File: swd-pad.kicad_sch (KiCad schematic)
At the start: 4 parts, among them J6 OroConn6p

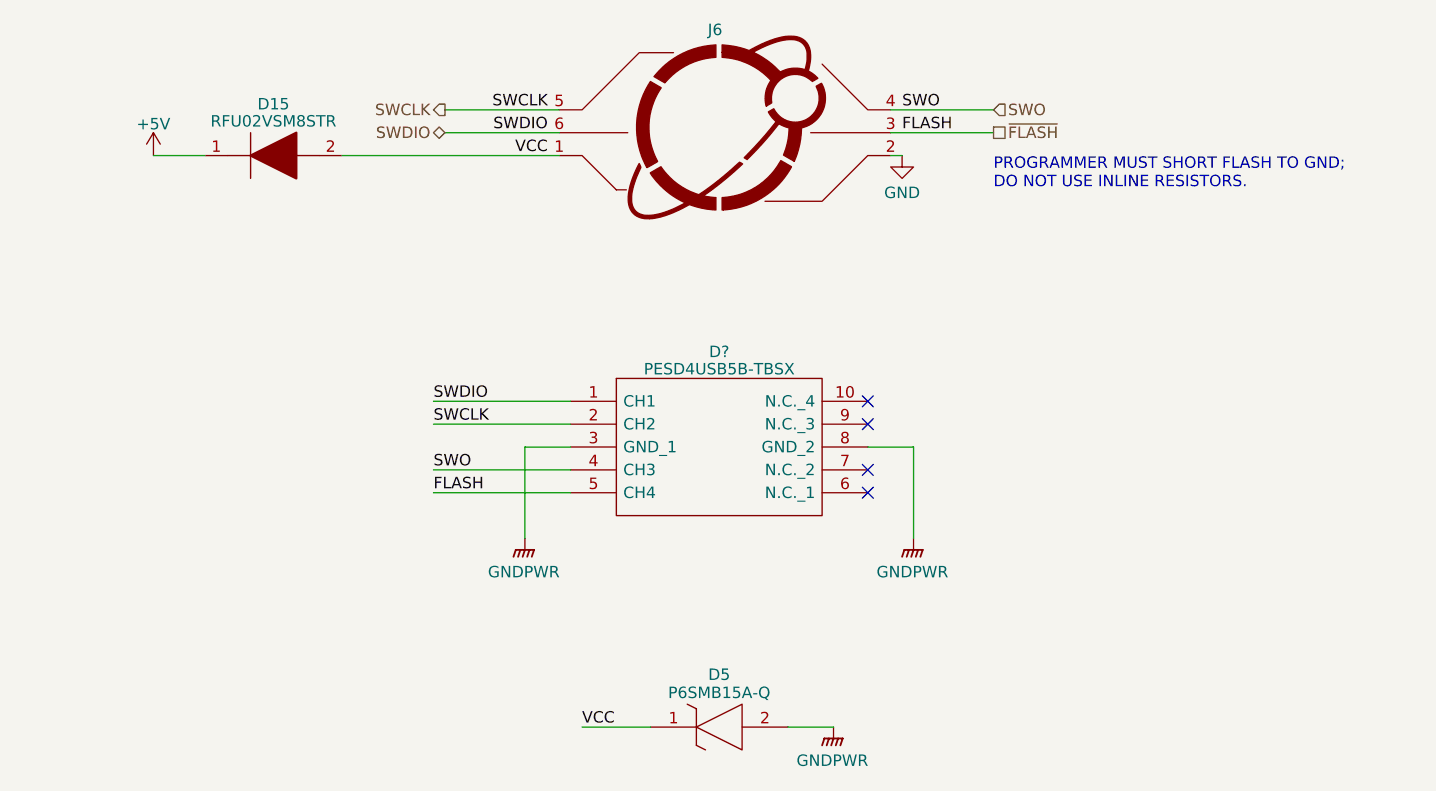
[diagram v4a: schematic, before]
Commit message: initial component layout
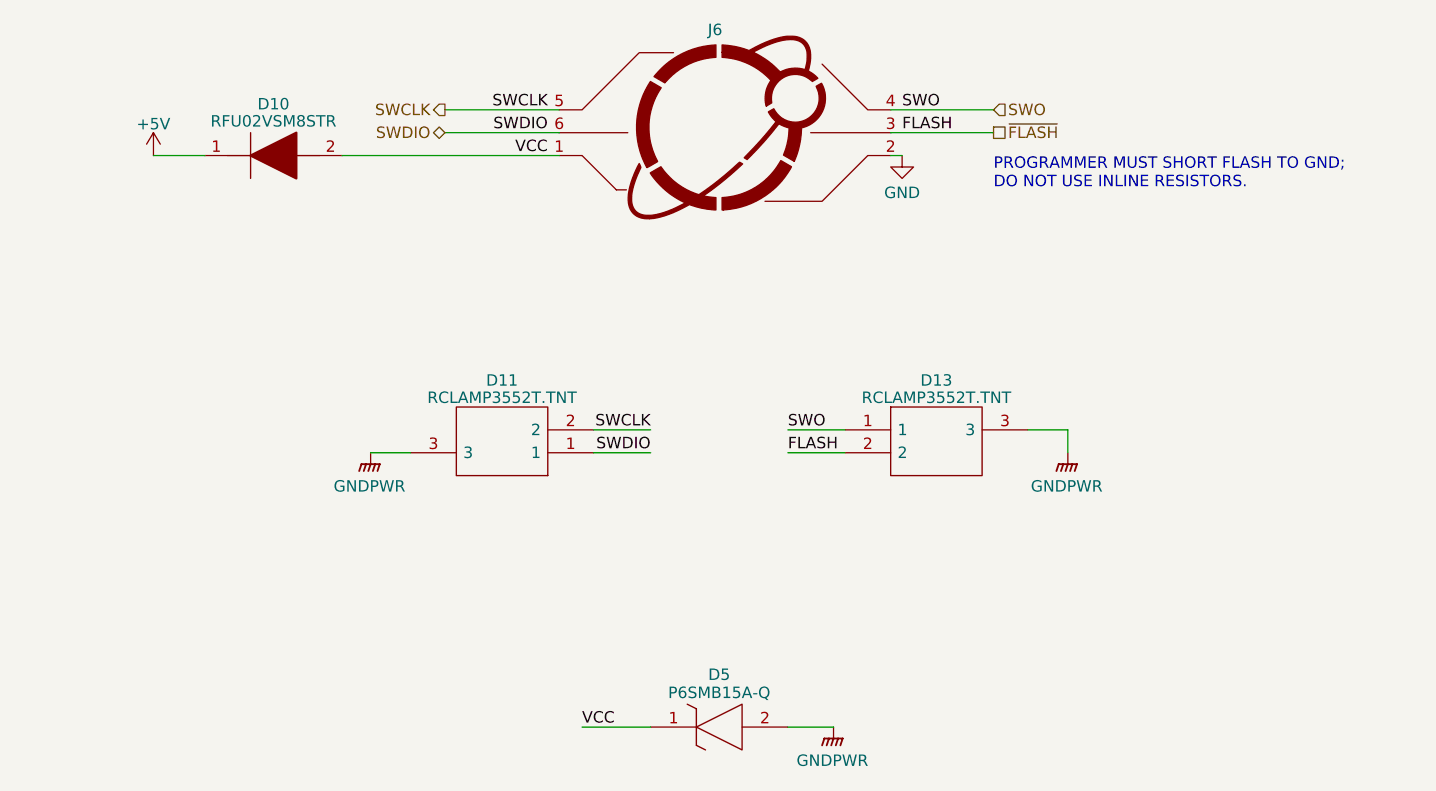
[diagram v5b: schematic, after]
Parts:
- removed D?: PESD4USB5B-TBSX, PESD4USB5BTBSX, symbol SamacSys_Parts:PESD4USB5B-TBSX
- added D11, D13: RCLAMP3552T.TNT, RCLAMP3552TTNT, symbol SamacSys_Parts:RCLAMP3552T.TNT
- renumbered D15 to D10
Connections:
- net GNDPWR: now also D11.3, D13.3
- net SWCLK: now also D11.2
- net SWDIO: now also D11.1
- net SWO: now also D13.1
- net ~{FLASH}: now also D13.2
- no-connect marks 4 -> 0
